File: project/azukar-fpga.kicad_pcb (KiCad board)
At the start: 2 copper layers, 100 x 75 mm, 155 parts, among them J1 USB_C_Receptacle_USB2.0_16P, P1 Conector 2x10, P2 Conector 2x10, P3 Conector 2x10, P4 Conector 2x10, SW1 SW_Push, SW2 SW_Push, SW3 SW_Push, SW4 SW_Push, SW5 SW_Push, SW6 SW_Push, SW7 SW_Push, SW8 SW_Push, U1 LD1117S33CTR, U2 LD1117S12CTR, U3 USBLC6-2SC6, U4 FT2232HL, U5 M93C66, U6 ICE40HX4K-TQ144, U7 W25X40CLSN, Y1 ECS-3225MV-120-CN-TR, Y2 ECS-3225MVQ-1000-CN-TR

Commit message: Version 2 de pcb completa, falta revisar silkscreen y ajustes menores
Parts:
- removed the C46 at (168.9, 104.8)
- removed the C47 at (168.9, 109.8)
- removed the C48 at (168.9, 102.3)
- removed the C49 at (161.3, 124.6)
- removed the C50 at (163.9, 124.6)
- removed the C51 at (158.8, 124.6)
- removed the C52 at (139.0, 104.6)
- removed the C53 at (139.0, 102.1)
- removed C54: 100n, Capacitor_SMD:C_1206_3216Metric
- removed the D4 at (168.0, 122.3)
- added C34: 1u, Capacitor_SMD:C_1206_3216Metric, F.Cu at (189.2, 124.2)
- added C35: 100n, Capacitor_SMD:C_1206_3216Metric, F.Cu at (189.2, 108.9)
- added C36: 100n, Capacitor_SMD:C_1206_3216Metric, F.Cu at (189.2, 121.8)
- added C37: 1u, Capacitor_SMD:C_1206_3216Metric, F.Cu at (158.8, 103.9)
- added C38: 100n, Capacitor_SMD:C_1206_3216Metric, F.Cu at (158.8, 108.6)
- added C39: 100n, Capacitor_SMD:C_1206_3216Metric, F.Cu at (158.8, 106.3)
- added C40: 1u, Capacitor_SMD:C_1206_3216Metric, F.Cu at (158.8, 123.4)
- added C41: 100n, Capacitor_SMD:C_1206_3216Metric, F.Cu at (158.8, 121.1)
- added D2: D_Schottky, Diode_SMD:D_1206_3216Metric_Pad1.42x1.75mm_HandSolder, F.Cu at (158.8, 125.8)
- added JP2: SolderJumper_2_Open, Jumper:SolderJumper-2_P1.3mm_Open_TrianglePad1.0x1.5mm, F.Cu at (176.8, 129.8)
- C20, C23: value 100n -> 10u
- C21, C24: value 10u -> 100n
- C25: value 100n -> 10n
- C26, C28: value 10n -> 1u
- C27: value 1u -> 10n
- C29: value 1u -> 100n
- D3: value D_Schottky -> LED Red; footprint Diode_SMD:D_1206_3216Metric_Pad1.42x1.75mm_HandSolder -> 150141RS73100(LED):LEDM3528X210N
- R10: value 2k2 -> 12k
- R11: value 100 -> 1k
- R14, R16: value 220 -> 100
- R15: value 220 -> 2k2
- R17, R18: value 220 -> 10k
- R5: value 12k -> 220
- R6: value 1k -> 220
- R7, R8: value 10k -> 220
- R9: value 100 -> 220
- TP1: footprint TestPoint:TestPoint_Pad_D2.5mm -> TestPoint:TestPoint_Pad_D1.5mm
- moved P1 99.3 mm to (126.9, 85.9), turned to 0 degrees
- moved P2 99.3 mm to (213.0, 135.4), turned to 180 degrees
- moved FFID1 96.4 mm to (226.4, 109.7)
- moved FFID5 88.8 mm to (110.6, 122.5)
- moved P3 86.2 mm to (213.0, 108.7), turned to 180 degrees
- moved P4 86.2 mm to (126.8, 112.5), turned to 0 degrees
- moved R22 58.0 mm to (143.4, 91.2), turned to 90 degrees
- moved C43 55.6 mm to (187.7, 130.7)
- moved C44 52.1 mm to (185.3, 130.7)
- moved R20 50.1 mm to (151.7, 96.0), turned to 180 degrees
- moved R23 49.8 mm to (153.9, 90.5)
- moved C27 46.9 mm to (145.3, 98.6), turned to 180 degrees
- moved C32 45.8 mm to (189.2, 111.3), turned to 0 degrees
- moved FB5 45.7 mm to (170.8, 83.4)
- moved C45 44.7 mm to (167.2, 130.7), turned to -90 degrees
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- renumbered BFID6 to BFID1, BFID7 to BFID2, BFID8 to BFID3, C34 to C46, C35 to C47, C36 to C48, C37 to C49, C38 to C50, C39 to C51, C40 to C52, C41 to C53, D2 to D1, D11 to D10, D12 to D11, D5 to D4, D6 to D5, D7 to D6, D8 to D7, D9 to D8, D10 to D9, P3 to P1, P1 to P2, P2 to P3
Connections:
- C17 pad 1: +3V3 -> +1V8
- C20 pad 1: +1V8 -> /Memorias y PLL/GNDPLL1
- C20 pad 2: GND -> /Memorias y PLL/VCCPLL1
- C22 pad 1: /Memorias y PLL/GNDPLL1 -> +3V3
- C22 pad 2: /Memorias y PLL/VCCPLL1 -> GND
- C23 pad 1: +3V3 -> /Memorias y PLL/VCCPLL2
- C23 pad 2: GND -> /Memorias y PLL/GNDPLL2
- C25 pad 1: /Memorias y PLL/VCCPLL2 -> +3V3
- C25 pad 2: /Memorias y PLL/GNDPLL2 -> GND
- C29 pad 1: +3V3 -> +1V2
- C33 pad 1: +1V2 -> +3V3
- D3 pad 1: Net-(D3-K) -> GND
- D3 pad 2: +3V3 -> Net-(D3-A)
- R10 pad 1: /Memorias y PLL/EEPROM_DATA -> GND
- R10 pad 2: Net-(U5-DO) -> Net-(U4-REF)
- R11 pad 1: +1V2 -> +3V3
- R11 pad 2: /Memorias y PLL/VCCPLL2 -> Net-(U4-~{RESET})
- R12 pad 2: Net-(U5-DO) -> /Memorias y PLL/EEPROM_CLK
- R13 pad 2: Net-(U6E-~{CRESET}) -> /Memorias y PLL/EEPROM_CS
- R14 pad 1: Net-(U6E-~{CRESET}) -> +1V2
- R14 pad 2: /Memorias y PLL/Flash_RESET -> /Memorias y PLL/VCCPLL1
- R15 pad 1: /Memorias y PLL/Flash_DI -> /Memorias y PLL/EEPROM_DATA
- R15 pad 2: Net-(U6E-IOB_105_SDO) -> Net-(U5-DO)
- R16 pad 1: /Memorias y PLL/Flash_DO -> +1V2
- R16 pad 2: Net-(U6E-IOB_106_SDI) -> /Memorias y PLL/VCCPLL2
- R17 pad 1: /Memorias y PLL/Flash_SCK -> +3V3
- R17 pad 2: Net-(U6E-IOB_107_SCK) -> Net-(U5-DO)
- R18 pad 1: /Memorias y PLL/Flash_CS -> +3V3
- R18 pad 2: Net-(U6E-IOB_108_SS) -> /Memorias y PLL/Flash_RESET
- R19 pad 2: Net-(U6E-IOB_108_SS) -> /Memorias y PLL/Flash_CS
- R20 pad 2: Net-(U6E-IOB_107_SCK) -> /Memorias y PLL/Flash_SCK
- R21 pad 2: Net-(D4-A) (its old number) -> Net-(D3-A)
- R24 pad 1: Net-(D4-A) (its old number) -> Net-(D3-A)
- R5 pad 1: GND -> /Memorias y PLL/Flash_SCK
- R5 pad 2: Net-(U4-REF) -> Net-(U4-ADBUS0)
- R6 pad 1: +3V3 -> Net-(U4-ADBUS1)
- R6 pad 2: Net-(U4-~{RESET}) -> /Memorias y PLL/Flash_DI
- R7 pad 1: +3V3 -> Net-(U4-ADBUS2)
- R7 pad 2: /Memorias y PLL/EEPROM_CLK -> /Memorias y PLL/Flash_DO
- R8 pad 1: +3V3 -> Net-(U4-ADBUS4)
- R8 pad 2: /Memorias y PLL/EEPROM_CS -> /Memorias y PLL/Flash_CS
- R9 pad 1: +1V2 -> Net-(U4-ADBUS7)
- R9 pad 2: /Memorias y PLL/VCCPLL1 -> /Memorias y PLL/Flash_RESET
- U4 pad 16: /Memorias y PLL/Flash_SCK -> Net-(U4-ADBUS0)
- U4 pad 17: /Memorias y PLL/Flash_DI -> Net-(U4-ADBUS1)
- U4 pad 18: /Memorias y PLL/Flash_DO -> Net-(U4-ADBUS2)
- U4 pad 21: /Memorias y PLL/Flash_CS -> Net-(U4-ADBUS4)
- U4 pad 24: /Memorias y PLL/Flash_RESET -> Net-(U4-ADBUS7)
- U6 pad 108: Net-(D3-K) -> Net-(D2-K)
- U6 pad 110: /Perifericos/LED1 -> /Perifericos/BOT1
- U6 pad 112: /Perifericos/LED2 -> /Perifericos/BOT2
- U6 pad 113: /Perifericos/LED3 -> /Perifericos/BOT3
- U6 pad 114: /Perifericos/LED4 -> /Perifericos/BOT4
- U6 pad 115: /Perifericos/LED5 -> /Perifericos/BOT5
- U6 pad 116: /Perifericos/LED6 -> /Perifericos/BOT6
- U6 pad 117: /Perifericos/LED7 -> /Perifericos/BOT7
- U6 pad 118: /Perifericos/LED8 -> /Perifericos/BOT8
- U6 pad 129: Net-(JP1-B) -> Net-(JP2-B)
- U6 pad 37: /Perifericos/BOT1 -> /Perifericos/LED1
- U6 pad 38: /Perifericos/BOT2 -> /Perifericos/LED2
- U6 pad 39: /Perifericos/BOT3 -> /Perifericos/LED3
- U6 pad 41: /Perifericos/BOT4 -> /Perifericos/LED4
- U6 pad 42: /Perifericos/BOT5 -> /Perifericos/LED5
- U6 pad 43: /Perifericos/BOT6 -> /Perifericos/LED6
- U6 pad 44: /Perifericos/BOT7 -> /Perifericos/LED7
- U6 pad 45: /Perifericos/BOT8 -> /Perifericos/LED8
- U6 pad 49: Net-(U6C-IOB_81_GBIN5) -> Net-(JP1-B)
- U6 pad 55: /Perifericos/VUART_Rx -> /Perifericos/VUART_DCD
- U6 pad 56: /Perifericos/VUART_Tx -> /Perifericos/VUART_DSR
- U6 pad 60: /Perifericos/VUART_RTS -> /Perifericos/VUART_DTR
- U6 pad 62: /Perifericos/VUART_DTR -> /Perifericos/VUART_RTS
- U6 pad 63: /Perifericos/VUART_DSR -> /Perifericos/VUART_Tx
- U6 pad 64: /Perifericos/VUART_DCD -> /Perifericos/VUART_Rx
- U6 pad 65: Net-(D4-A) (its old number) -> Net-(D3-A)
- U6 pad 66: Net-(U6E-~{CRESET}) -> /Memorias y PLL/Flash_RESET
- U6 pad 67: Net-(U6E-IOB_105_SDO) -> /Memorias y PLL/Flash_DI
- U6 pad 68: Net-(U6E-IOB_106_SDI) -> /Memorias y PLL/Flash_DO
- U6 pad 70: Net-(U6E-IOB_107_SCK) -> /Memorias y PLL/Flash_SCK
- U6 pad 71: Net-(U6E-IOB_108_SS) -> /Memorias y PLL/Flash_CS
- U7 pad 1: Net-(U6E-IOB_108_SS) -> /Memorias y PLL/Flash_CS
- U7 pad 2: Net-(U6E-IOB_106_SDI) -> /Memorias y PLL/Flash_DO
- U7 pad 5: Net-(U6E-IOB_105_SDO) -> /Memorias y PLL/Flash_DI
- U7 pad 6: Net-(U6E-IOB_107_SCK) -> /Memorias y PLL/Flash_SCK
- Y2 pad 3: Net-(U6C-IOB_81_GBIN5) -> /Perifericos/100MHz_CLK
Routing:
- net Net-(U6E-~{CRESET}): track 101.0 -> 0.00 mm, vias 5 -> 0
- net Net-(U6E-IOB_107_SCK): track 89.9 -> 0.00 mm, vias 5 -> 0
- net Net-(U6E-IOB_105_SDO): track 89.4 -> 0.00 mm, vias 6 -> 0
- net GND: track 502.0 -> 426.3 mm, vias 52 -> 43
- net Net-(U6E-IOB_108_SS): track 64.7 -> 0.00 mm, vias 4 -> 0
- net Net-(U6E-IOB_106_SDI): track 63.7 -> 0.00 mm, vias 4 -> 0
- net /Perifericos/VUART_DSR: track 77.6 -> 14.4 mm
- net /Perifericos/VUART_DCD: track 76.2 -> 16.0 mm
- net /Perifericos/VUART_DTR: track 72.9 -> 16.7 mm
- net /Perifericos/VUART_Tx: track 70.3 -> 17.3 mm
- net /Perifericos/VUART_CTS: track 68.7 -> 15.8 mm
- net /Perifericos/VUART_Rx: track 64.7 -> 15.4 mm, vias 4 -> 2
- net /Perifericos/VUART_RTS: track 65.2 -> 17.4 mm
- net /Memorias y PLL/Flash_DO: track 82.7 -> 35.6 mm
- net /Memorias y PLL/Flash_CS: track 81.4 -> 36.4 mm, vias 2 -> 3
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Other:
- board text added: "0"
- board text added: "0 mm"
- board text added: "0.01 mm"
- board text added: "0.02"
- board text added: "0.035 mm"
- board text added: "0.2000 mm / 0.2000 mm"
- board text added: "0.3000 mm"
- board text added: "1"
- board text added: "1.51 mm"
- board text added: "1.6000 mm"
- board text added: "100.0000 mm x 75.0000 mm"
- board text added: "2"
- board text added: "3.3"
- board text added: "4.5"
- board text added: "B.Cu"
- board text added: "B.Mask"
- board text added: "B.Paste"
- board text added: "B.Silkscreen"
- board text added: "BOARD CHARACTERISTICS"
- board text added: "Board Thickness:"
- board text added: "Board overall dimensions:"
- board text added: "Bottom Silk Screen"
- board text added: "Bottom Solder Mask"
- board text added: "Bottom Solder Paste"
- board text added: "Castellated pads:"
- board text added: "Color"
- board text added: "Copper Finish:"
- board text added: "Copper Layer Count:"
- board text added: "Dielectric"
- board text added: "Edge card connectors:"
- board text added: "Epsilon R"
- board text added: "F.Cu"
- board text added: "F.Mask"
- board text added: "F.Paste"
- board text added: "F.Silkscreen"
- board text added: "FR4"
- board text added: "Impedance Control:"
- board text added: "Layer Name"
- board text added: "Loss Tangent"
- board text added: "Material"
- board text added: "Min hole diameter:"
- board text added: "Min track/spacing:"
- board text added: "No"
- board text added: "None"
- board text added: "Not specified"
- board text added: "Plated Board Edge:"
- board text added: "Thickness (mm)"
- board text added: "Top Silk Screen"
- board text added: "Top Solder Mask"
- board text added: "Top Solder Paste"
- board text added: "Type"
- board text added: "copper"
- board text added: "core"

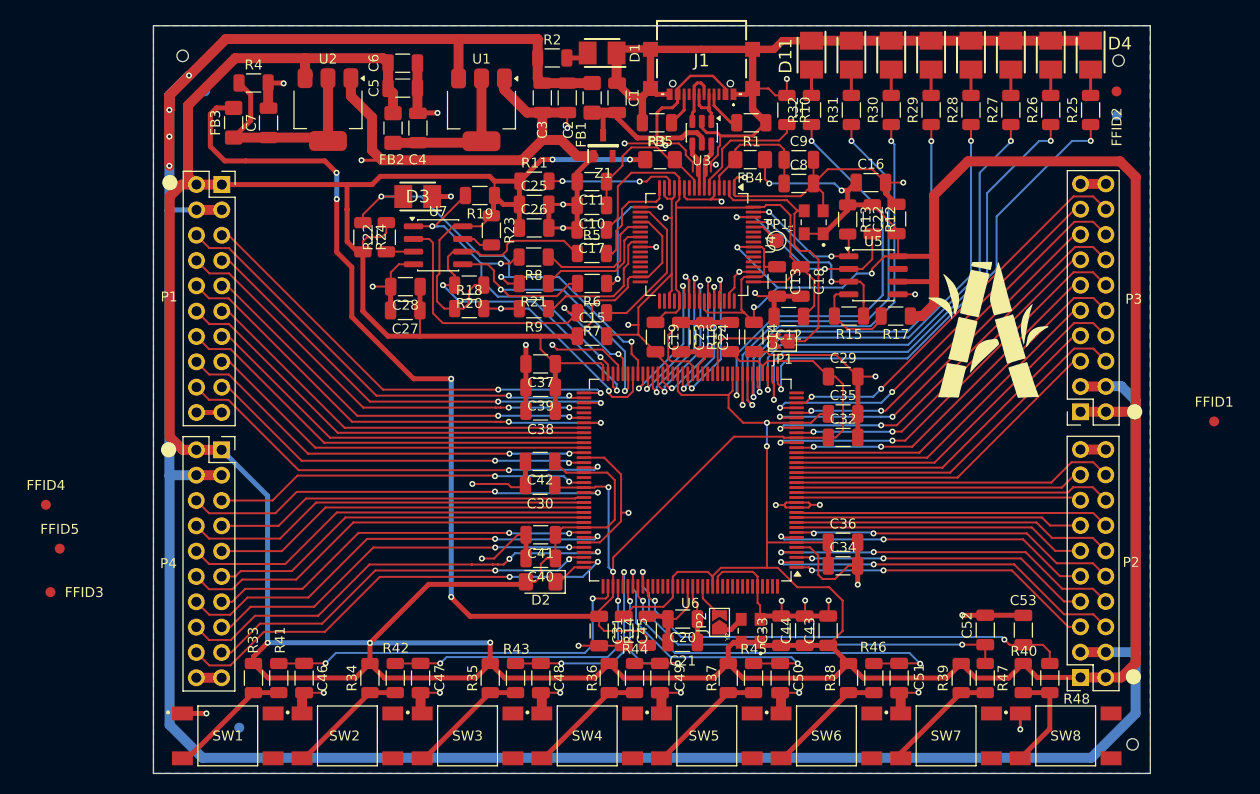
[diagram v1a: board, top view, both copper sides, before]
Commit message: actualizados anchos de pistas de potencia
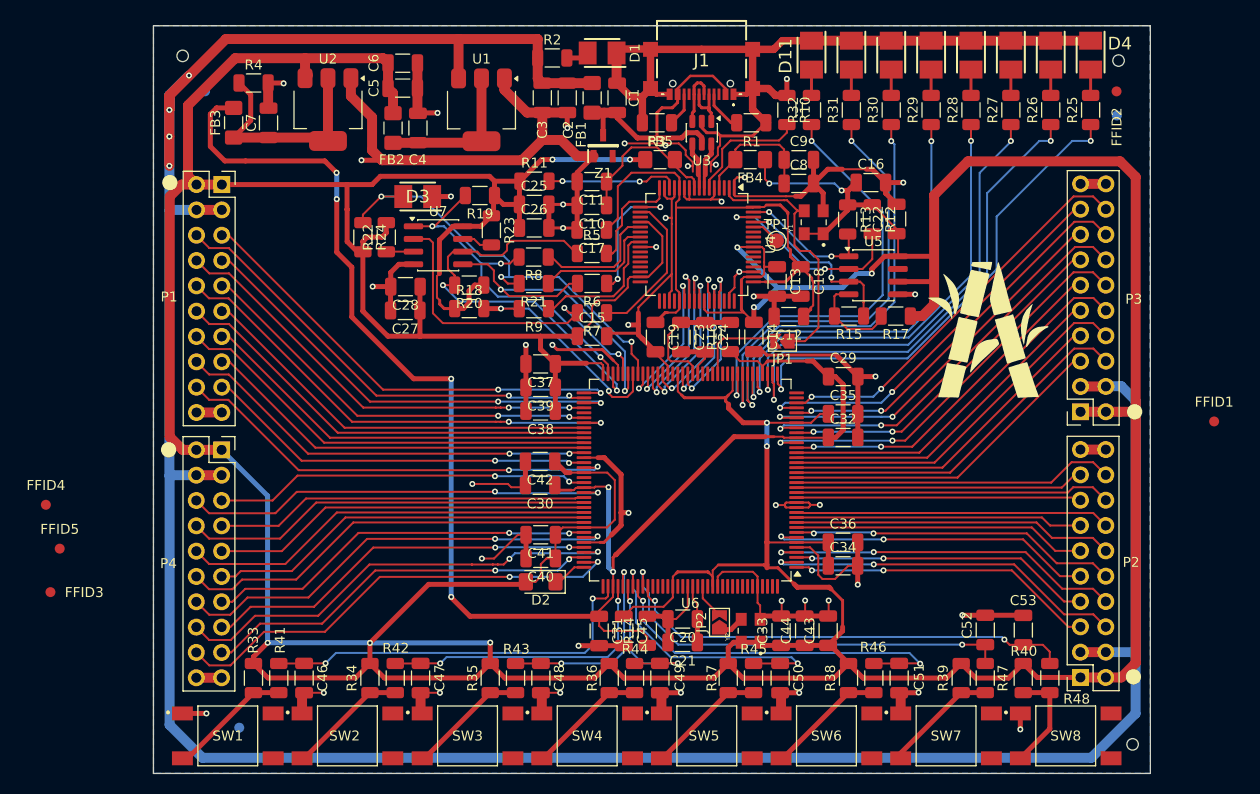
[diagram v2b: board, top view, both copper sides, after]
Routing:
- net GND: track 426.3 -> 428.3 mm, vias 43 -> 44
- net +3V3: track 681.3 -> 683.1 mm

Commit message: Deleting old files
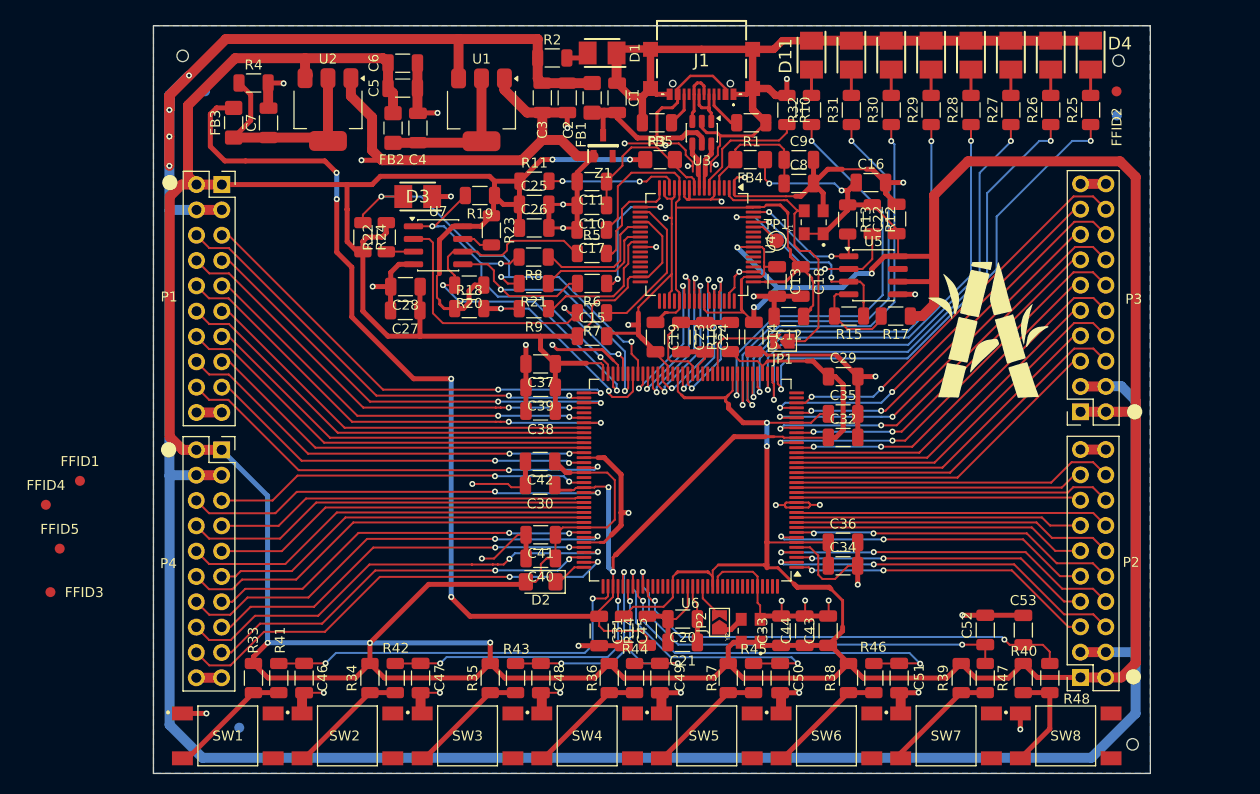
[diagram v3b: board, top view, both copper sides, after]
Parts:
- moved FFID1 113.9 mm to (112.6, 115.7)
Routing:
- net GND: track 428.3 -> 429.7 mm
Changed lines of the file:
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@@
 	(footprint "Fiducial:Fiducial_1mm_Mask2mm"
 		(layer "F.Cu")
-		(at 226.4 109.69)
+		(at 112.63 115.65)
 		(descr "Fiducial, circular marking, 1mm bare copper, 2mm soldermask opening (Level A)")
 		(tags "fiducial")
@@
 	)
 	(segment
+		(start 173.76 87.42)
+		(end 173.51 87.42)
+		(width 0.2)
+		(layer "F.Cu")
+		(net 1)
+	)
+	(segment
 		(start 214.308 71.4964)
 		(end 214.008 71.4964)
@@
 	(segment
 		(start 175.913824 87.42)
-		(end 173.736 87.42)
+		(end 173.76 87.42)
 		(width 0.2)
 		(layer "F.Cu")
@@
 		(layer "F.Cu")
 		(net 1)
+	)
+	(segment
+		(start 173.76 86.265)
+		(end 173.76 87.42)
+		(width 0.2)
+		(layer "F.Cu")
+		(net 1)

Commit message: Reordenadas las resistencias y capacitores de los botones y separaciones
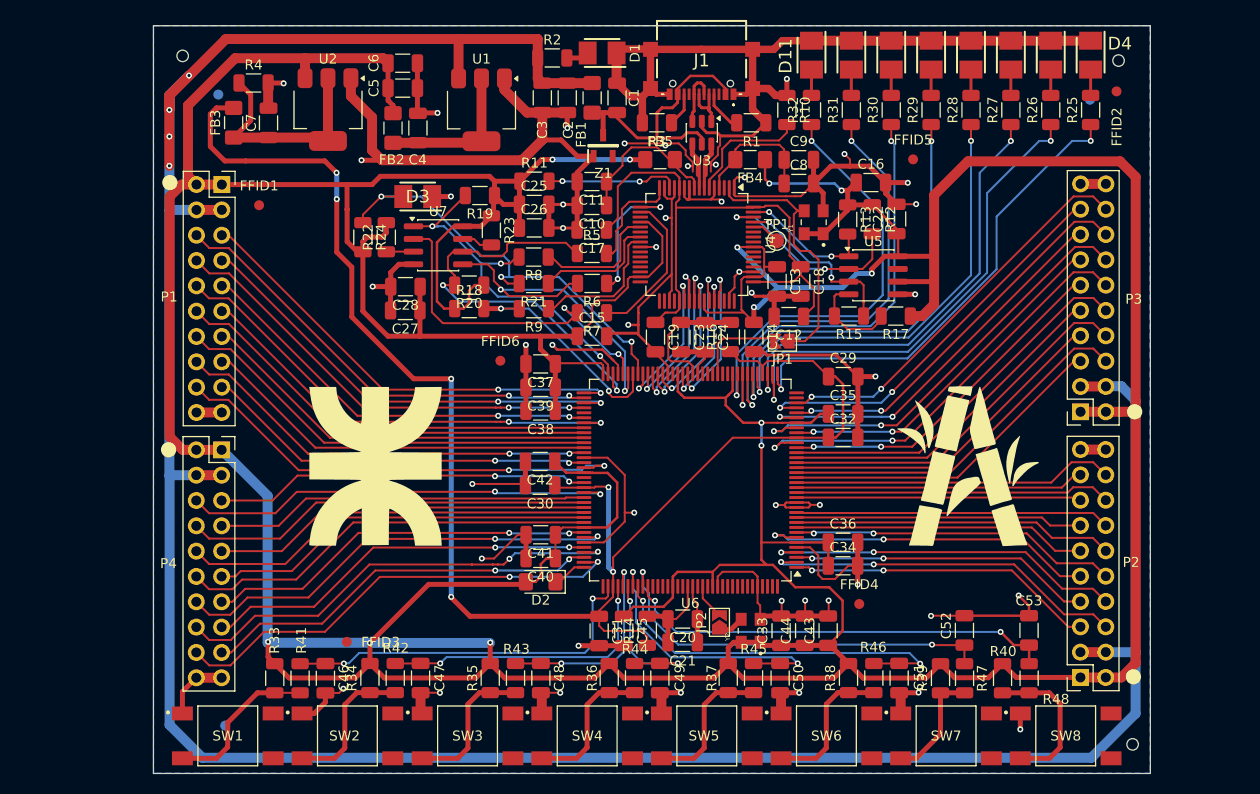
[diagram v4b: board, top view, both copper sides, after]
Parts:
- added FFID6: Fiducial, Fiducial:Fiducial_1mm_Mask2mm, F.Cu at (154.8, 103.6)
- moved BFID1 108.4 mm to (127.2, 140.2)
- moved BFID3 106.1 mm to (213.9, 77.4)
- moved FFID5 94.1 mm to (196.2, 83.4)
- moved FFID4 82.2 mm to (190.8, 128.0)
- moved FFID1 33.0 mm to (130.6, 88.0)
- moved FFID3 30.1 mm to (139.4, 131.8)
- moved REF** 4.25 mm to (207.4, 79.6)
- moved C46 2.14 mm to (137.2, 135.4)
- moved R33 2.14 mm to (132.2, 135.4)
- moved R41 2.14 mm to (134.7, 135.4)
- moved C52 2.09 mm to (201.3, 130.7)
- moved R39 2.08 mm to (198.9, 135.4)
- moved R40 2.08 mm to (205.2, 135.4)
- moved R47 2.08 mm to (201.4, 135.4)
- moved R48 2.08 mm to (207.8, 135.4)
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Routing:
- net GND: track 429.7 -> 444.2 mm, vias 44 -> 46
- net Net-(R40-Pad2): track 10.5 -> 15.1 mm
- net Net-(R33-Pad2): track 12.4 -> 16.5 mm
- net +3V3: track 683.1 -> 679.2 mm
- net Net-(R38-Pad2): track 12.0 -> 14.6 mm
- net Net-(R35-Pad2): track 12.1 -> 14.7 mm
- net Net-(R37-Pad2): track 12.0 -> 14.5 mm
- net Net-(R34-Pad2): track 12.1 -> 14.6 mm
- net Net-(R36-Pad2): track 12.0 -> 14.5 mm
- net /Perifericos/BOT1: track 39.5 -> 37.4 mm
- net /Perifericos/BOT7: track 42.9 -> 40.8 mm
- net /Perifericos/BOT8: track 45.4 -> 43.7 mm
- net Net-(P3-IO8): track 42.0 -> 43.6 mm
- net Net-(P3-IO10): track 42.4 -> 43.9 mm
- net Net-(P1-IO14): track 45.3 -> 46.7 mm
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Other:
- board text added: "AZUKAR FPGA Version 2.0 - 2026 CERN-OHL-P-2.0 © M. Simonazzi, V. Gomez Espeche"
- board text removed: "AZUKAR FPGA Version 1.4 - 2026 CERN-OHL-P-2.0 © M. Simonazzi, V. Gomez Espeche"

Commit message: Corregida serigrafia frontal, modificada serigrafia trasera
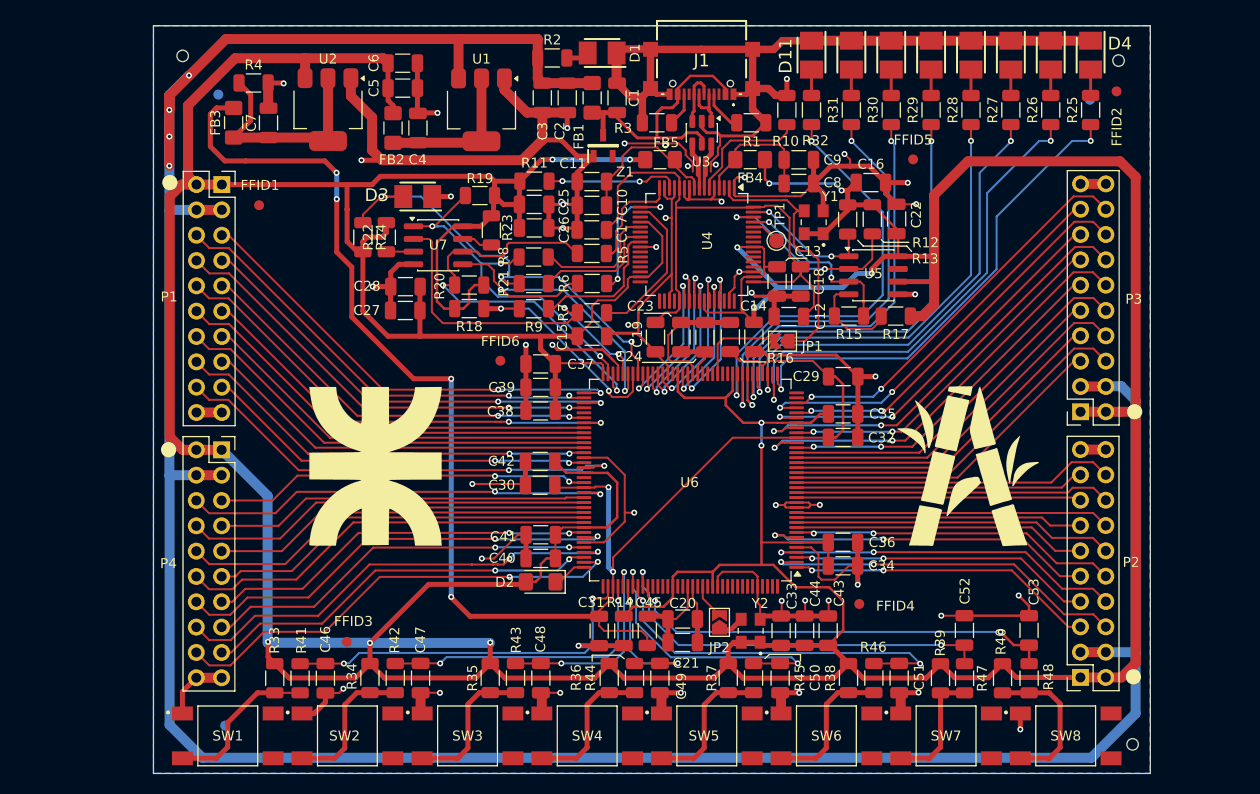
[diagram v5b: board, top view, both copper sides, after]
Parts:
- added kibuzzard-69B0D836: G***, kibuzzard-69B0D836, B.Cu at (208.2, 112.4)
- added kibuzzard-69B0D836: G***, kibuzzard-69B0D836, B.Cu at (208.2, 85.9)
- added kibuzzard-69B0D8FC: G***, kibuzzard-69B0D8FC, B.Cu at (208.3, 106.2)
- added kibuzzard-69B0D906: G***, kibuzzard-69B0D906, B.Cu at (208.3, 108.7)
- added kibuzzard-69B0D94C: G***, kibuzzard-69B0D94C, B.Cu at (208.1, 132.9)
- added kibuzzard-69B0D951: G***, kibuzzard-69B0D951, B.Cu at (208.1, 135.4)
- added kibuzzard-69B0D982: G***, kibuzzard-69B0D982, B.Cu at (132.0, 108.7)
- added kibuzzard-69B0D982: G***, kibuzzard-69B0D982, B.Cu at (132.1, 135.4)
- added kibuzzard-69B0DA46: G***, kibuzzard-69B0DA46, B.Cu at (132.1, 112.6)
- added kibuzzard-69B0DA4D: G***, kibuzzard-69B0DA4D, B.Cu at (132.1, 115.1)
- added kibuzzard-69B0DA56: G***, kibuzzard-69B0DA56, B.Cu at (132.1, 85.9)
- added kibuzzard-69B0DA5B: G***, kibuzzard-69B0DA5B, B.Cu at (132.0, 88.4)
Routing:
- net GND: track 444.2 -> 443.4 mm
- net Net-(R39-Pad2): track 11.5 -> 12.3 mm
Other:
- board text removed: "+3V3"
- board text removed: "+5V"
- board text removed: "GND"
